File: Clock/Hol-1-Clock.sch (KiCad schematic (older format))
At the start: 18 parts, among them P1 CONN_2, P2 CONN_1, P3 CONN_1, SW1 SW_PUSH, U1 NE555, U2 NE555

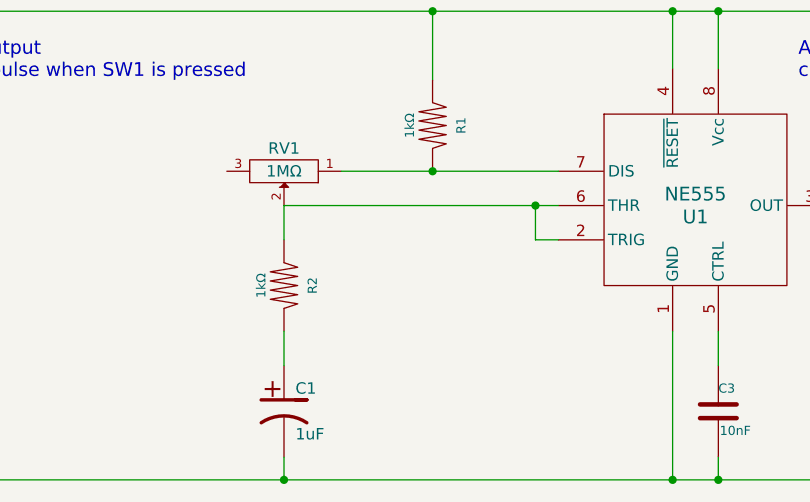
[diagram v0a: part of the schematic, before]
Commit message: v1.4.1 pcb layout for clock sources
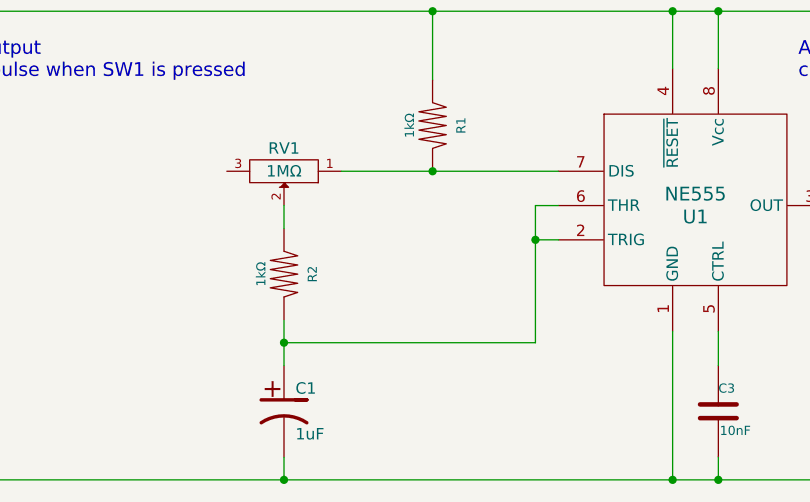
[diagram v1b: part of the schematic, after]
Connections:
- net at U1.2 (TRIG), U1.6 (THR): now also C1.1, R2.2; no longer R2.1, RV1.2
- new net: R2.1, RV1.2
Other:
- moved on the sheet: R2
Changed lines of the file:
@@
 L R R2
 U 1 1 5C9BFAE4
-P 5650 2050
-F 0 "R2" V 5775 2050 40  0000 C CNN
-F 1 "1kΩ" V 5550 2050 40  0000 C CNN
-F 2 "~" V 5580 2050 30  0000 C CNN
-F 3 "~" H 5650 2000 30  0000 C CNN
-	1    5650 2050
+P 5650 2000
+F 0 "R2" V 5775 2000 40  0000 C CNN
+F 1 "1kΩ" V 5550 2000 40  0000 C CNN
+F 2 "~" V 5580 2000 30  0000 C CNN
+F 3 "~" H 5650 1950 30  0000 C CNN
+	1    5650 2000
 	1    0    0    -1
 $EndComp
@@
 	5900 1550 6850 1550
 Wire Wire Line
-	5650 1850 5650 1700
+	5650 1800 5650 1700
 Connection ~ 6300 1550
-Wire Wire Line
-	5650 1700 6850 1700
-Wire Wire Line
-	6850 1850 6750 1850
-Wire Wire Line
-	6750 1850 6750 1700
-Connection ~ 6750 1700
 $Comp
 L C C3
@@
 Connection ~ 5650 2900
 Wire Wire Line
-	5650 2400 5650 2250
+	5650 2400 5650 2200
 $Comp
 L CONN_1 P2
@@
 Text Notes 6850 700  0    60   ~ 0
 CLOCK SOURCE B
+Wire Wire Line
+	5650 2300 6750 2300
+Wire Wire Line
+	6750 2300 6750 1700
+Wire Wire Line
+	6750 1700 6850 1700
+Connection ~ 5650 2300
+Wire Wire Line
+	6850 1850 6750 1850
+Connection ~ 6750 1850
 $EndSCHEMATC
